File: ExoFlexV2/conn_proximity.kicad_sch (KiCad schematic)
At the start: 40 parts

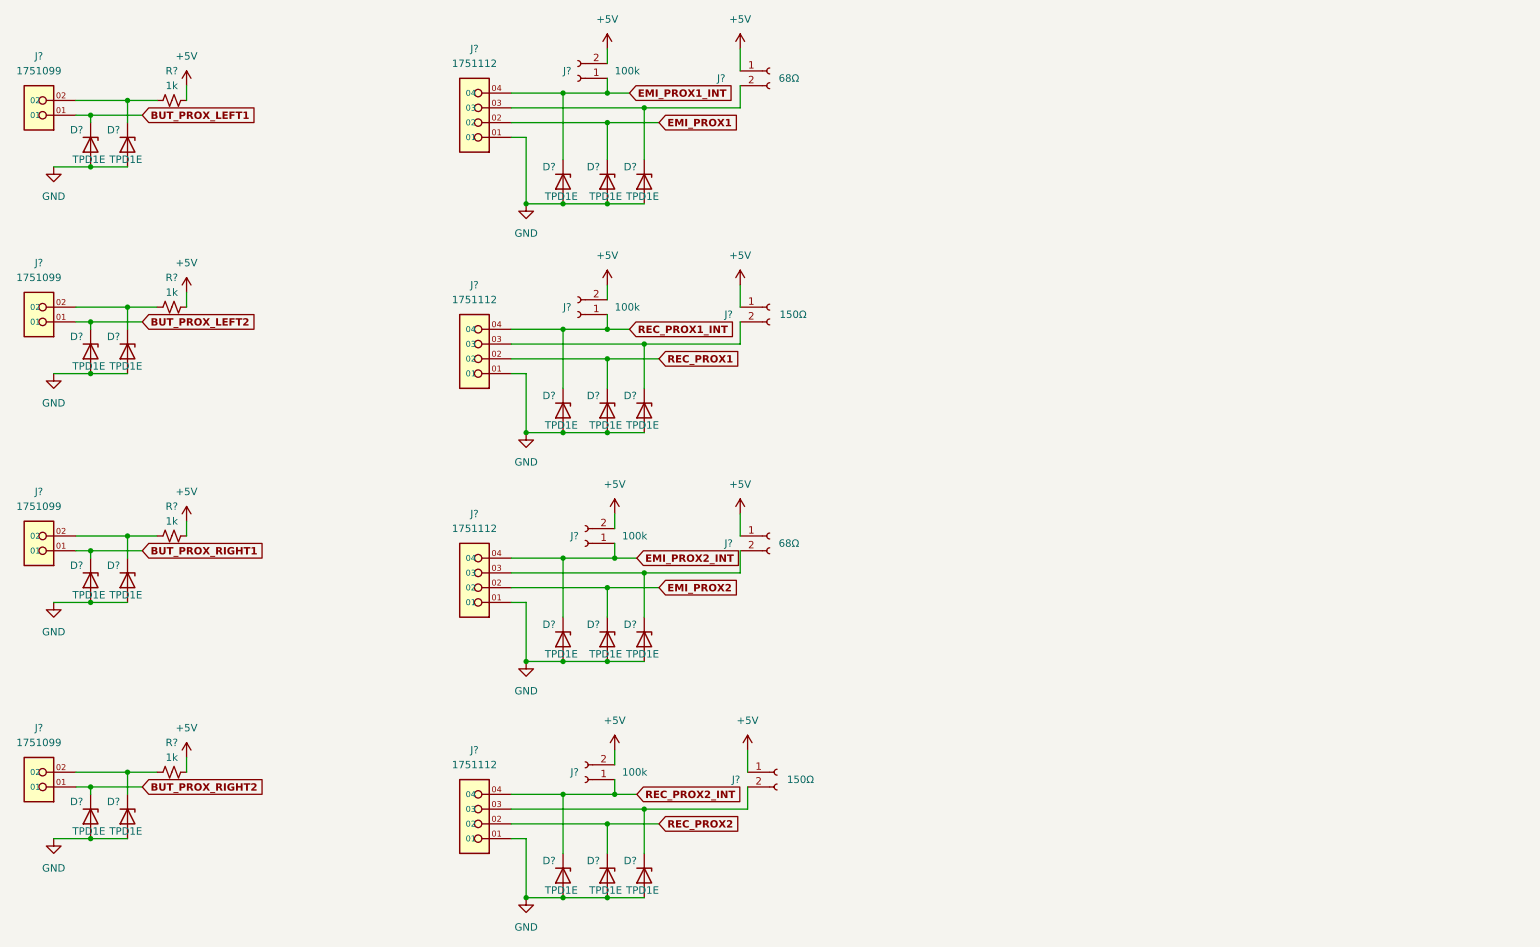
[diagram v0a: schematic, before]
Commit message: Mise à jour signaux STM
- Condo de découplage
- Signaux supplémentaire pour le STM
- Page GND sera pour Multiplexeur
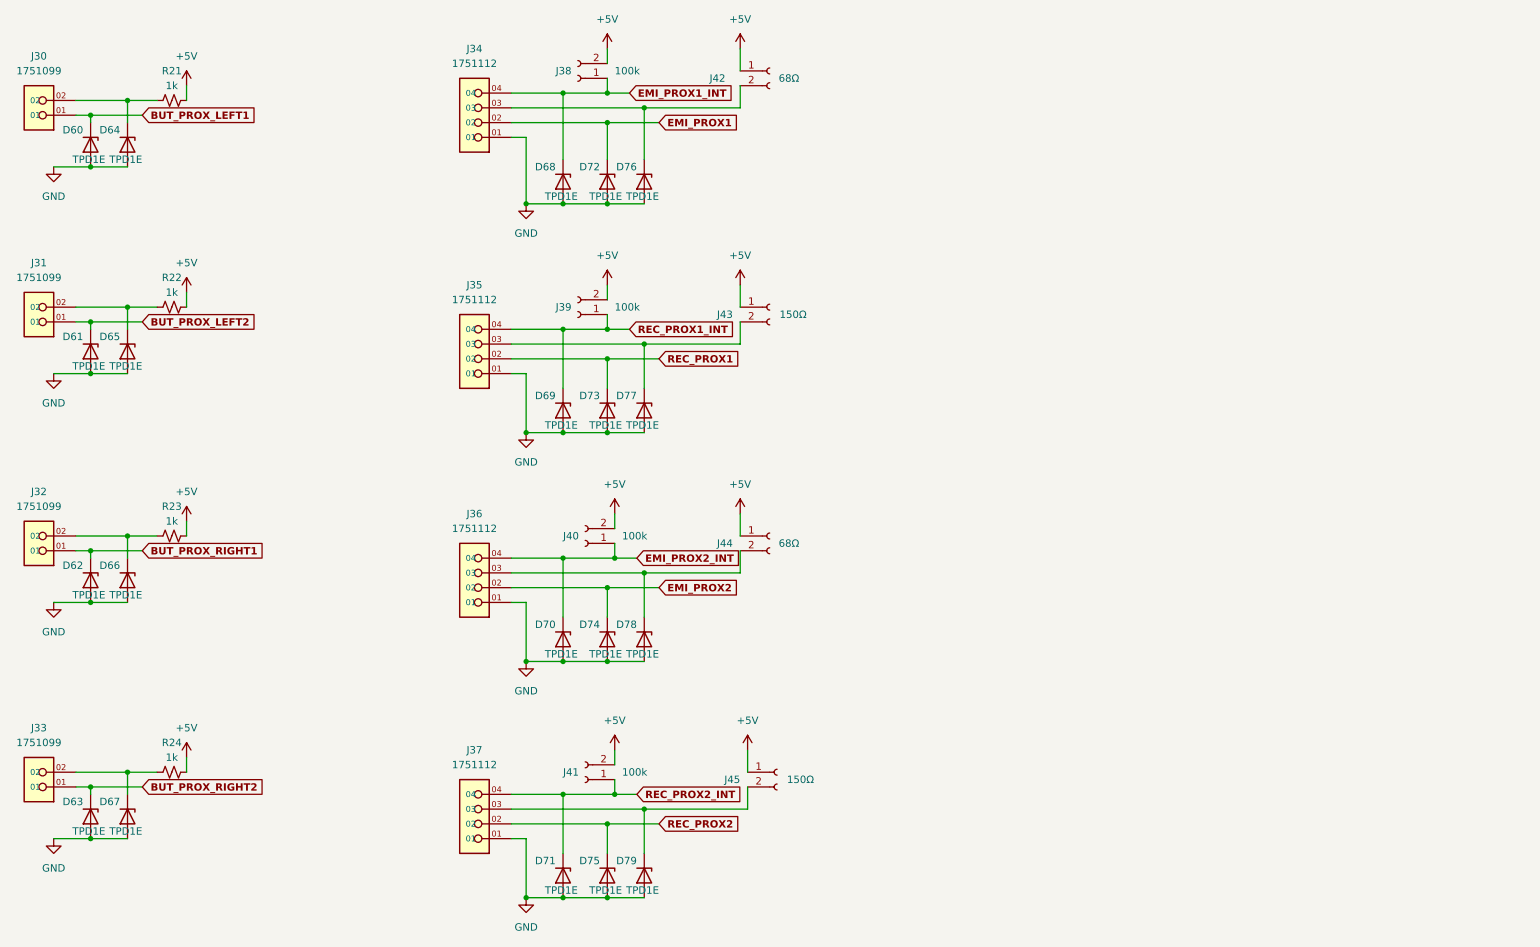
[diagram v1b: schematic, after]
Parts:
- gave numbers to parts that had none: 40

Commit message: Finalisation 1
- Ajout de pages pour la gestion des signaux négatif
- Modification des pages de torque et amplitude
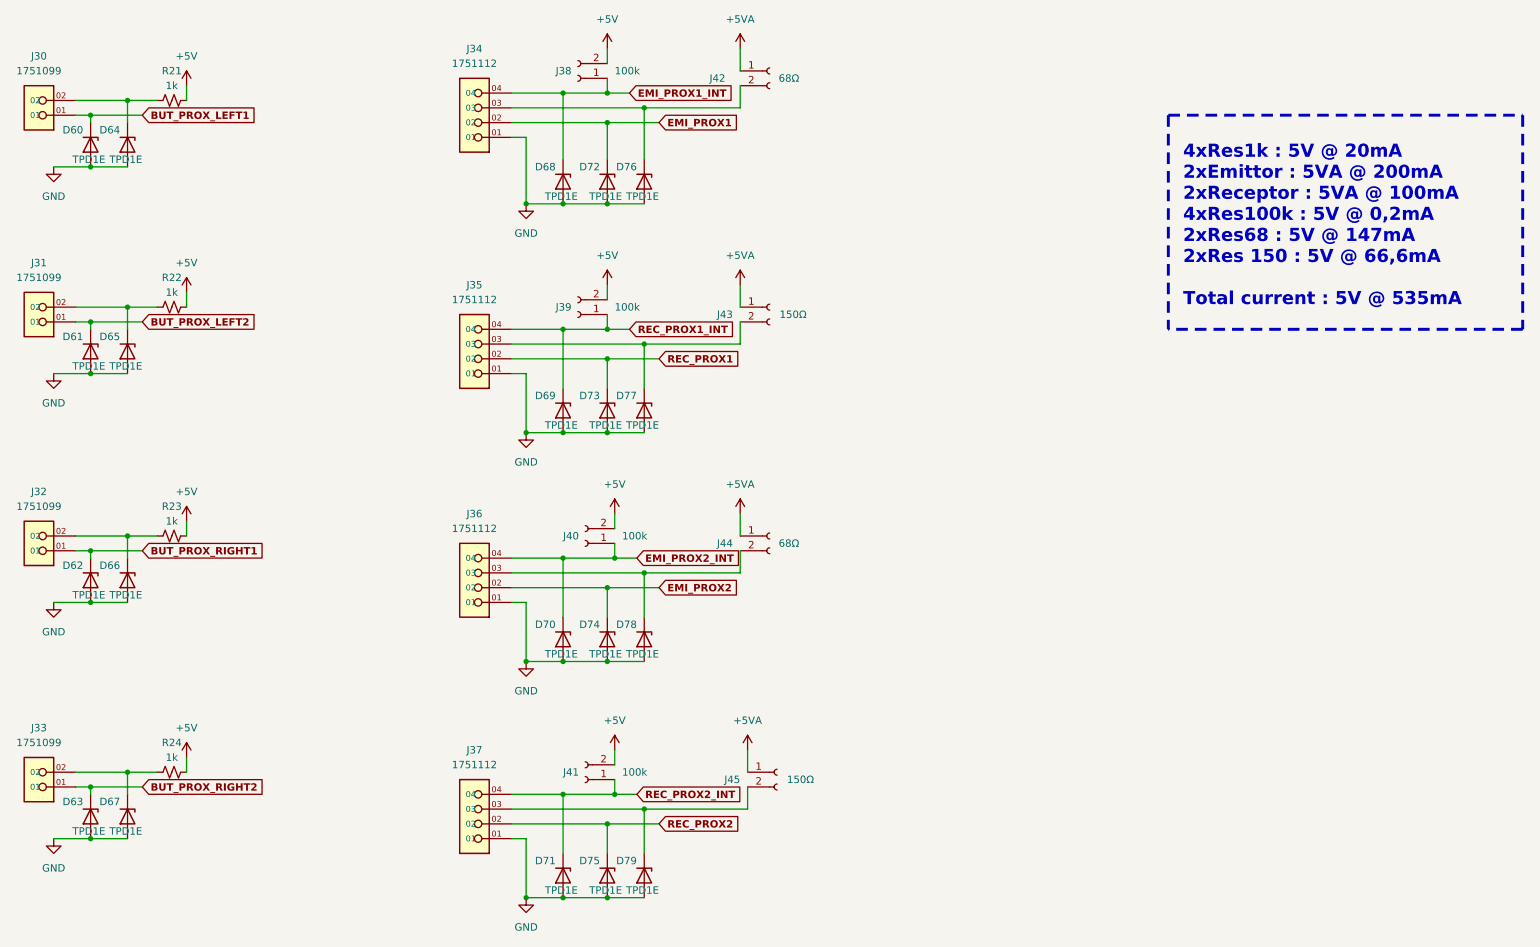
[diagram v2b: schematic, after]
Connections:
- net +5V: no longer J42.1 (Pin_1), J43.1 (Pin_1), J44.1 (Pin_1), J45.1 (Pin_1)
- new net +5VA: J42.1 (Pin_1), J43.1 (Pin_1), J44.1 (Pin_1), J45.1 (Pin_1)
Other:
- note added: "4xRes1k : 5V @ 20mA 2xEmittor : 5VA @ 200mA 2xReceptor : 5VA @ 100mA 4xRes100k : 5V @ 0,2mA 2xRes68 : 5V @ 147mA 2xRes 150 : 5V @ 66,6mA Total current : 5V @ 535mA"
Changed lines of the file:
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@@
     (stroke (width 0) (type default) (color 0 0 0 0))
+  )
+  (polyline (pts (xy 283.21 33.02) (xy 283.21 69.85))
+    (stroke (width 0.5) (type dash) (color 255 148 44 1))
   )
   (wire (pts (xy 125.73 74.93) (xy 109.22 74.93))
@@
     (stroke (width 0) (type default) (color 0 0 0 0))
   )
+  (polyline (pts (xy 222.25 33.02) (xy 283.21 33.02))
+    (stroke (width 0.5) (type dash) (color 255 148 44 1))
+  )
   (wire (pts (xy 118.11 69.85) (xy 109.22 69.85))
     (stroke (width 0) (type default) (color 0 0 0 0))
@@
     (stroke (width 0) (type default) (color 0 0 0 0))
   )
+  (polyline (pts (xy 283.21 69.85) (xy 222.25 69.85))
+    (stroke (width 0.5) (type dash) (color 255 148 44 1))
+  )
   (wire (pts (xy 36.83 116.84) (xy 43.18 116.84))
     (stroke (width 0) (type default) (color 0 0 0 0))
@@
     (stroke (width 0) (type default) (color 0 0 0 0))
   )
+  (polyline (pts (xy 222.25 33.02) (xy 222.25 69.85))
+    (stroke (width 0.5) (type dash) (color 255 148 44 1))
+  )
   (wire (pts (xy 125.73 69.85) (xy 129.54 69.85))
     (stroke (width 0) (type default) (color 0 0 0 0))
@@
   (wire (pts (xy 111.76 87.63) (xy 118.11 87.63))
     (stroke (width 0) (type default) (color 0 0 0 0))
+  )
+  (text "4xRes1k : 5V @ 20mA\n2xEmittor : 5VA @ 200mA\n2xReceptor : 5VA @ 100mA\n4xRes100k : 5V @ 0,2mA\n2xRes68 : 5V @ 147mA\n2xRes 150 : 5V @ 66,6mA\n\nTotal current : 5V @ 535mA"
+    (at 224.79 66.04 0)
+    (effects (font (size 2.25 2.25) (thickness 0.5) bold) (justify left bottom))
   )
   (global_label "REC_PROX1" (shape input) (at 134.62 74.93 0) (fields_autoplaced)
@@
     (pin "04")
   )
+  (symbol (lib_id "power:+5VA") (at 148.59 62.23 0) (unit 1)
+    (in_bom yes) (on_board yes) (fields_autoplaced)
+    (property "Reference" "#PWR?" (id 0) (at 148.59 66.04 0)
+      (effects (font (size 1.27 1.27)) hide)
+    )
+    (property "Value" "+5VA" (id 1) (at 148.59 57.15 0))
+    (property "Footprint" "" (id 2) (at 148.59 62.23 0)
+      (effects (font (size 1.27 1.27)) hide)
+    )
+    (property "Datasheet" "" (id 3) (at 148.59 62.23 0)
+      (effects (font (size 1.27 1.27)) hide)
+    )
+    (pin "1")
+  )
   (symbol (lib_id "Device:D_Zener") (at 43.18 113.03 270) (unit 1)
     (in_bom yes) (on_board yes)
@@
     (pin "1")
     (pin "2")
-  )
-  (symbol (lib_id "power:+5V") (at 149.86 142.24 0) (unit 1)
-    (in_bom yes) (on_board yes) (fields_autoplaced)
-    (property "Reference" "#PWR092" (id 0) (at 149.86 146.05 0)
-      (effects (font (size 1.27 1.27)) hide)
-    )
-    (property "Value" "+5V" (id 1) (at 149.86 137.16 0))
-    (property "Footprint" "" (id 2) (at 149.86 142.24 0)
-      (effects (font (size 1.27 1.27)) hide)
-    )
-    (property "Datasheet" "" (id 3) (at 149.86 142.24 0)
-      (effects (font (size 1.27 1.27)) hide)
-    )
-    (pin "1")
   )
   (symbol (lib_id "power:GND") (at 111.76 127 0) (unit 1)
@@
     (pin "2")
   )
+  (symbol (lib_id "power:+5VA") (at 148.59 21.59 0) (unit 1)
+    (in_bom yes) (on_board yes) (fields_autoplaced)
+    (property "Reference" "#PWR?" (id 0) (at 148.59 25.4 0)
+      (effects (font (size 1.27 1.27)) hide)
+    )
+    (property "Value" "+5VA" (id 1) (at 148.59 16.51 0))
+    (property "Footprint" "" (id 2) (at 148.59 21.59 0)
+      (effects (font (size 1.27 1.27)) hide)
+    )
+    (property "Datasheet" "" (id 3) (at 148.59 21.59 0)
+      (effects (font (size 1.27 1.27)) hide)
+    )
+    (pin "1")
+  )
   (symbol (lib_id "power:GND") (at 30.48 157.48 0) (unit 1)
     (in_bom yes) (on_board yes) (fields_autoplaced)
@@
     )
     (property "Datasheet" "" (id 3) (at 53.34 102.87 0)
+      (effects (font (size 1.27 1.27)) hide)
+    )
+    (pin "1")
+  )
+  (symbol (lib_id "power:+5VA") (at 148.59 101.6 0) (unit 1)
+    (in_bom yes) (on_board yes) (fields_autoplaced)
+    (property "Reference" "#PWR?" (id 0) (at 148.59 105.41 0)
+      (effects (font (size 1.27 1.27)) hide)
+    )
+    (property "Value" "+5VA" (id 1) (at 148.59 96.52 0))
+    (property "Footprint" "" (id 2) (at 148.59 101.6 0)
+      (effects (font (size 1.27 1.27)) hide)
+    )
+    (property "Datasheet" "" (id 3) (at 148.59 101.6 0)
       (effects (font (size 1.27 1.27)) hide)
     )
@@
     (pin "04")
   )
-  (symbol (lib_id "power:+5V") (at 148.59 62.23 0) (unit 1)
-    (in_bom yes) (on_board yes) (fields_autoplaced)
-    (property "Reference" "#PWR090" (id 0) (at 148.59 66.04 0)
-      (effects (font (size 1.27 1.27)) hide)
-    )
-    (property "Value" "+5V" (id 1) (at 148.59 57.15 0))
-    (property "Footprint" "" (id 2) (at 148.59 62.23 0)
-      (effects (font (size 1.27 1.27)) hide)
-    )
-    (property "Datasheet" "" (id 3) (at 148.59 62.23 0)
-      (effects (font (size 1.27 1.27)) hide)
-    )
-    (pin "1")
-  )
-  (symbol (lib_id "power:+5V") (at 148.59 101.6 0) (unit 1)
-    (in_bom yes) (on_board yes) (fields_autoplaced)
-    (property "Reference" "#PWR091" (id 0) (at 148.59 105.41 0)
-      (effects (font (size 1.27 1.27)) hide)
-    )
-    (property "Value" "+5V" (id 1) (at 148.59 96.52 0))
-    (property "Footprint" "" (id 2) (at 148.59 101.6 0)
-      (effects (font (size 1.27 1.27)) hide)
-    )
-    (property "Datasheet" "" (id 3) (at 148.59 101.6 0)
+  (symbol (lib_id "power:+5VA") (at 149.86 142.24 0) (unit 1)
+    (in_bom yes) (on_board yes) (fields_autoplaced)
+    (property "Reference" "#PWR?" (id 0) (at 149.86 146.05 0)
+      (effects (font (size 1.27 1.27)) hide)
+    )
+    (property "Value" "+5VA" (id 1) (at 149.86 137.16 0))
+    (property "Footprint" "" (id 2) (at 149.86 142.24 0)
+      (effects (font (size 1.27 1.27)) hide)
+    )
+    (property "Datasheet" "" (id 3) (at 149.86 142.24 0)
       (effects (font (size 1.27 1.27)) hide)
     )
@@
       (effects (font (size 1.27 1.27)) hide)
     )
-    (pin "1")
-  )
-  (symbol (lib_id "power:+5V") (at 148.59 21.59 0) (unit 1)
-    (in_bom yes) (on_board yes) (fields_autoplaced)
-    (property "Reference" "#PWR089" (id 0) (at 148.59 25.4 0)
-      (effects (font (size 1.27 1.27)) hide)
-    )
-    (property "Value" "+5V" (id 1) (at 148.59 16.51 0))
-    (property "Footprint" "" (id 2) (at 148.59 21.59 0)
-      (effects (font (size 1.27 1.27)) hide)
-    )
-    (property "Datasheet" "" (id 3) (at 148.59 21.59 0)
-      (effects (font (size 1.27 1.27)) hide)
-    )
